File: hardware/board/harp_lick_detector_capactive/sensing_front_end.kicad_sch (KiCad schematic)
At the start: 23 parts

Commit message: loosely place components
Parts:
- C32, C33, C34, C35: Link https://www.digikey.com/en/products/detail/samsung-electro-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 -> https://www.digikey.com/en/products/detail/walsin-technolog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; Manufacturer Samsung Electro-Mechanics -> Walson Technology Corporation; Manufacturer Number CL10B104KB8NNWC -> 0402B104K160CT; Rated Voltage 50V -> 16V
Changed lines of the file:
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@@
       (effects (font (size 1.27 1.27)) hide)
     )
-    (property "Datasheet" "https://media.digikey.com/pdf/Data%20Sheets/Samsung%20PDFs/CL10B104KB8NNWC_Spec.pdf" (id 3) (at 24.13 172.72 0)
-      (effects (font (size 1.27 1.27)) hide)
-    )
-    (property "Link" "https://www.digikey.com/en/products/detail/samsung-electro-mechanics/CL10B104KB8NNWC/3887593" (id 4) (at 24.13 172.72 0)
-      (effects (font (size 1.27 1.27)) hide)
-    )
-    (property "Manufacturer" "Samsung Electro-Mechanics" (id 5) (at 24.13 172.72 0)
-      (effects (font (size 1.27 1.27)) hide)
-    )
-    (property "Manufacturer Number" "CL10B104KB8NNWC" (id 6) (at 24.13 172.72 0)
-      (effects (font (size 1.27 1.27)) hide)
-    )
-    (property "Rated Voltage" "50V" (id 7) (at 24.13 172.72 0)
+    (property "Datasheet" "http://www.passivecomponent.com/wp-content/uploads/datasheet/WTC_MLCC_General_Purpose.pdf" (id 3) (at 24.13 172.72 0)
+      (effects (font (size 1.27 1.27)) hide)
+    )
+    (property "Link" "https://www.digikey.com/en/products/detail/walsin-technology-corporation/0402B104K160CT/6707534" (id 4) (at 24.13 172.72 0)
+      (effects (font (size 1.27 1.27)) hide)
+    )
+    (property "Manufacturer" "Walson Technology Corporation" (id 5) (at 24.13 172.72 0)
+      (effects (font (size 1.27 1.27)) hide)
+    )
+    (property "Manufacturer Number" "0402B104K160CT" (id 6) (at 24.13 172.72 0)
+      (effects (font (size 1.27 1.27)) hide)
+    )
+    (property "Rated Voltage" "16V" (id 7) (at 24.13 172.72 0)
       (effects (font (size 1.27 1.27)) hide)
     )
@@
       (effects (font (size 1.27 1.27)) hide)
     )
-    (property "Datasheet" "https://media.digikey.com/pdf/Data%20Sheets/Samsung%20PDFs/CL10B104KB8NNWC_Spec.pdf" (id 3) (at 53.34 172.72 0)
-      (effects (font (size 1.27 1.27)) hide)
-    )
-    (property "Link" "https://www.digikey.com/en/products/detail/samsung-electro-mechanics/CL10B104KB8NNWC/3887593" (id 4) (at 53.34 172.72 0)
-      (effects (font (size 1.27 1.27)) hide)
-    )
-    (property "Manufacturer" "Samsung Electro-Mechanics" (id 5) (at 53.34 172.72 0)
-      (effects (font (size 1.27 1.27)) hide)
-    )
-    (property "Manufacturer Number" "CL10B104KB8NNWC" (id 6) (at 53.34 172.72 0)
-      (effects (font (size 1.27 1.27)) hide)
-    )
-    (property "Rated Voltage" "50V" (id 7) (at 53.34 172.72 0)
+    (property "Datasheet" "http://www.passivecomponent.com/wp-content/uploads/datasheet/WTC_MLCC_General_Purpose.pdf" (id 3) (at 53.34 172.72 0)
+      (effects (font (size 1.27 1.27)) hide)
+    )
+    (property "Link" "https://www.digikey.com/en/products/detail/walsin-technology-corporation/0402B104K160CT/6707534" (id 4) (at 53.34 172.72 0)
+      (effects (font (size 1.27 1.27)) hide)
+    )
+    (property "Manufacturer" "Walson Technology Corporation" (id 5) (at 53.34 172.72 0)
+      (effects (font (size 1.27 1.27)) hide)
+    )
+    (property "Manufacturer Number" "0402B104K160CT" (id 6) (at 53.34 172.72 0)
+      (effects (font (size 1.27 1.27)) hide)
+    )
+    (property "Rated Voltage" "16V" (id 7) (at 53.34 172.72 0)
       (effects (font (size 1.27 1.27)) hide)
     )
@@
       (effects (font (size 1.27 1.27)) hide)
     )
-    (property "Datasheet" "https://media.digikey.com/pdf/Data%20Sheets/Samsung%20PDFs/CL10B104KB8NNWC_Spec.pdf" (id 3) (at 53.34 182.88 0)
-      (effects (font (size 1.27 1.27)) hide)
-    )
-    (property "Link" "https://www.digikey.com/en/products/detail/samsung-electro-mechanics/CL10B104KB8NNWC/3887593" (id 4) (at 53.34 182.88 0)
-      (effects (font (size 1.27 1.27)) hide)
-    )
-    (property "Manufacturer" "Samsung Electro-Mechanics" (id 5) (at 53.34 182.88 0)
-      (effects (font (size 1.27 1.27)) hide)
-    )
-    (property "Manufacturer Number" "CL10B104KB8NNWC" (id 6) (at 53.34 182.88 0)
-      (effects (font (size 1.27 1.27)) hide)
-    )
-    (property "Rated Voltage" "50V" (id 7) (at 53.34 182.88 0)
+    (property "Datasheet" "http://www.passivecomponent.com/wp-content/uploads/datasheet/WTC_MLCC_General_Purpose.pdf" (id 3) (at 53.34 182.88 0)
+      (effects (font (size 1.27 1.27)) hide)
+    )
+    (property "Link" "https://www.digikey.com/en/products/detail/walsin-technology-corporation/0402B104K160CT/6707534" (id 4) (at 53.34 182.88 0)
+      (effects (font (size 1.27 1.27)) hide)
+    )
+    (property "Manufacturer" "Walson Technology Corporation" (id 5) (at 53.34 182.88 0)
+      (effects (font (size 1.27 1.27)) hide)
+    )
+    (property "Manufacturer Number" "0402B104K160CT" (id 6) (at 53.34 182.88 0)
+      (effects (font (size 1.27 1.27)) hide)
+    )
+    (property "Rated Voltage" "16V" (id 7) (at 53.34 182.88 0)
       (effects (font (size 1.27 1.27)) hide)
     )
@@
       (effects (font (size 1.27 1.27)) hide)
     )
-    (property "Datasheet" "https://media.digikey.com/pdf/Data%20Sheets/Samsung%20PDFs/CL10B104KB8NNWC_Spec.pdf" (id 3) (at 24.13 182.88 0)
-      (effects (font (size 1.27 1.27)) hide)
-    )
-    (property "Link" "https://www.digikey.com/en/products/detail/samsung-electro-mechanics/CL10B104KB8NNWC/3887593" (id 4) (at 24.13 182.88 0)
-      (effects (font (size 1.27 1.27)) hide)
-    )
-    (property "Manufacturer" "Samsung Electro-Mechanics" (id 5) (at 24.13 182.88 0)
-      (effects (font (size 1.27 1.27)) hide)
-    )
-    (property "Manufacturer Number" "CL10B104KB8NNWC" (id 6) (at 24.13 182.88 0)
-      (effects (font (size 1.27 1.27)) hide)
-    )
-    (property "Rated Voltage" "50V" (id 7) (at 24.13 182.88 0)
-      (effects (font (size 1.27 1.27)) hide)
-    )
+    (property "Datasheet" "http://www.passivecomponent.com/wp-content/uploads/datasheet/WTC_MLCC_General_Purpose.pdf" (id 3) (at 24.13 182.88 0)
+      (effects (font (size 1.27 1.27)) hide)
+    )
+    (property "Link" "https://www.digikey.com/en/products/detail/walsin-technology-corporation/0402B104K160CT/6707534" (id 4) (at 24.13 182.88 0)
+      (effects (font (size 1.27 1.27)) hide)
+    )
+    (property "Manufacturer" "Walson Technology Corporation" (id 5) (at 24.13 182.88 0)
+      (effects (font (size 1.27 1.27)) hide)
+    )
+    (property "Manufacturer Number" "0402B104K160CT" (id 6) (at 24.13 182.88 0)
+      (effects (font (size 1.27 1.27)) hide)
+    )
+    (property "Rated Voltage" "16V" (id 7) (at 24.13 182.88 0)
+      (effects (font (size 1.27 1.27)) hide)
+    )

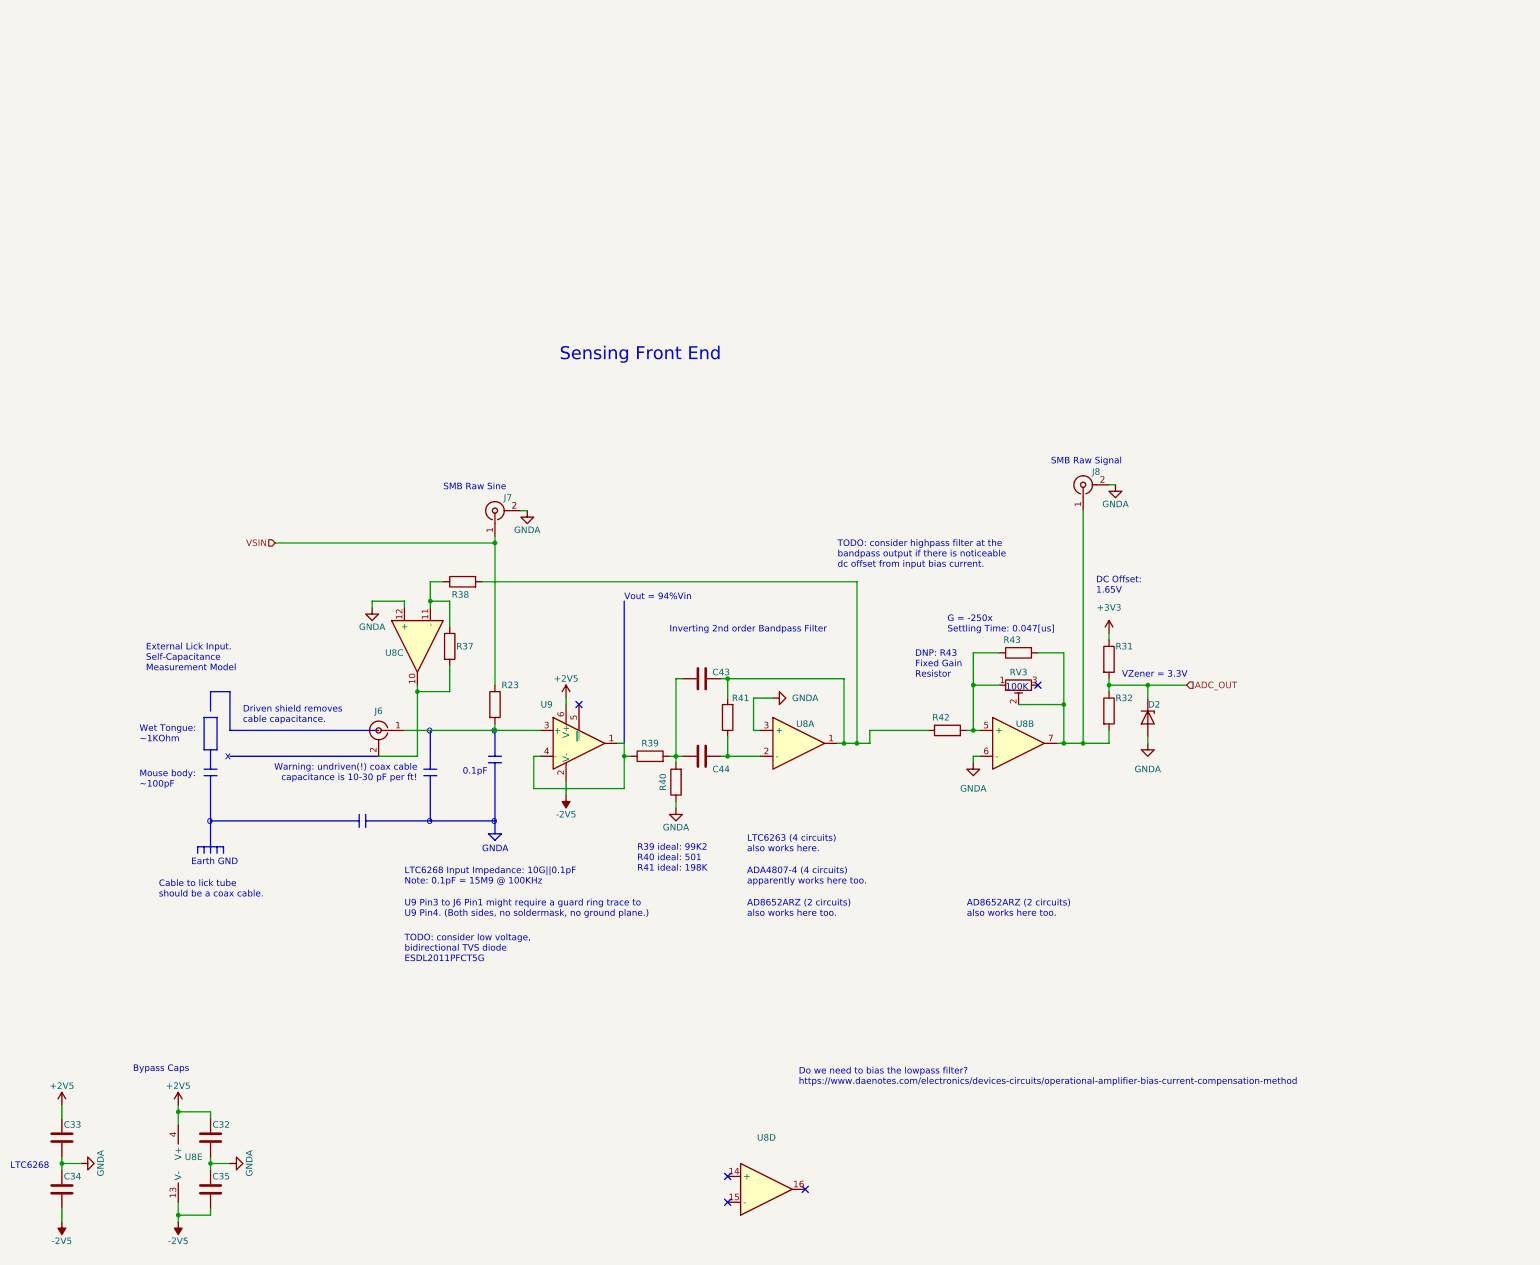
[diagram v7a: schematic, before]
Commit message: change usb connector; more layout
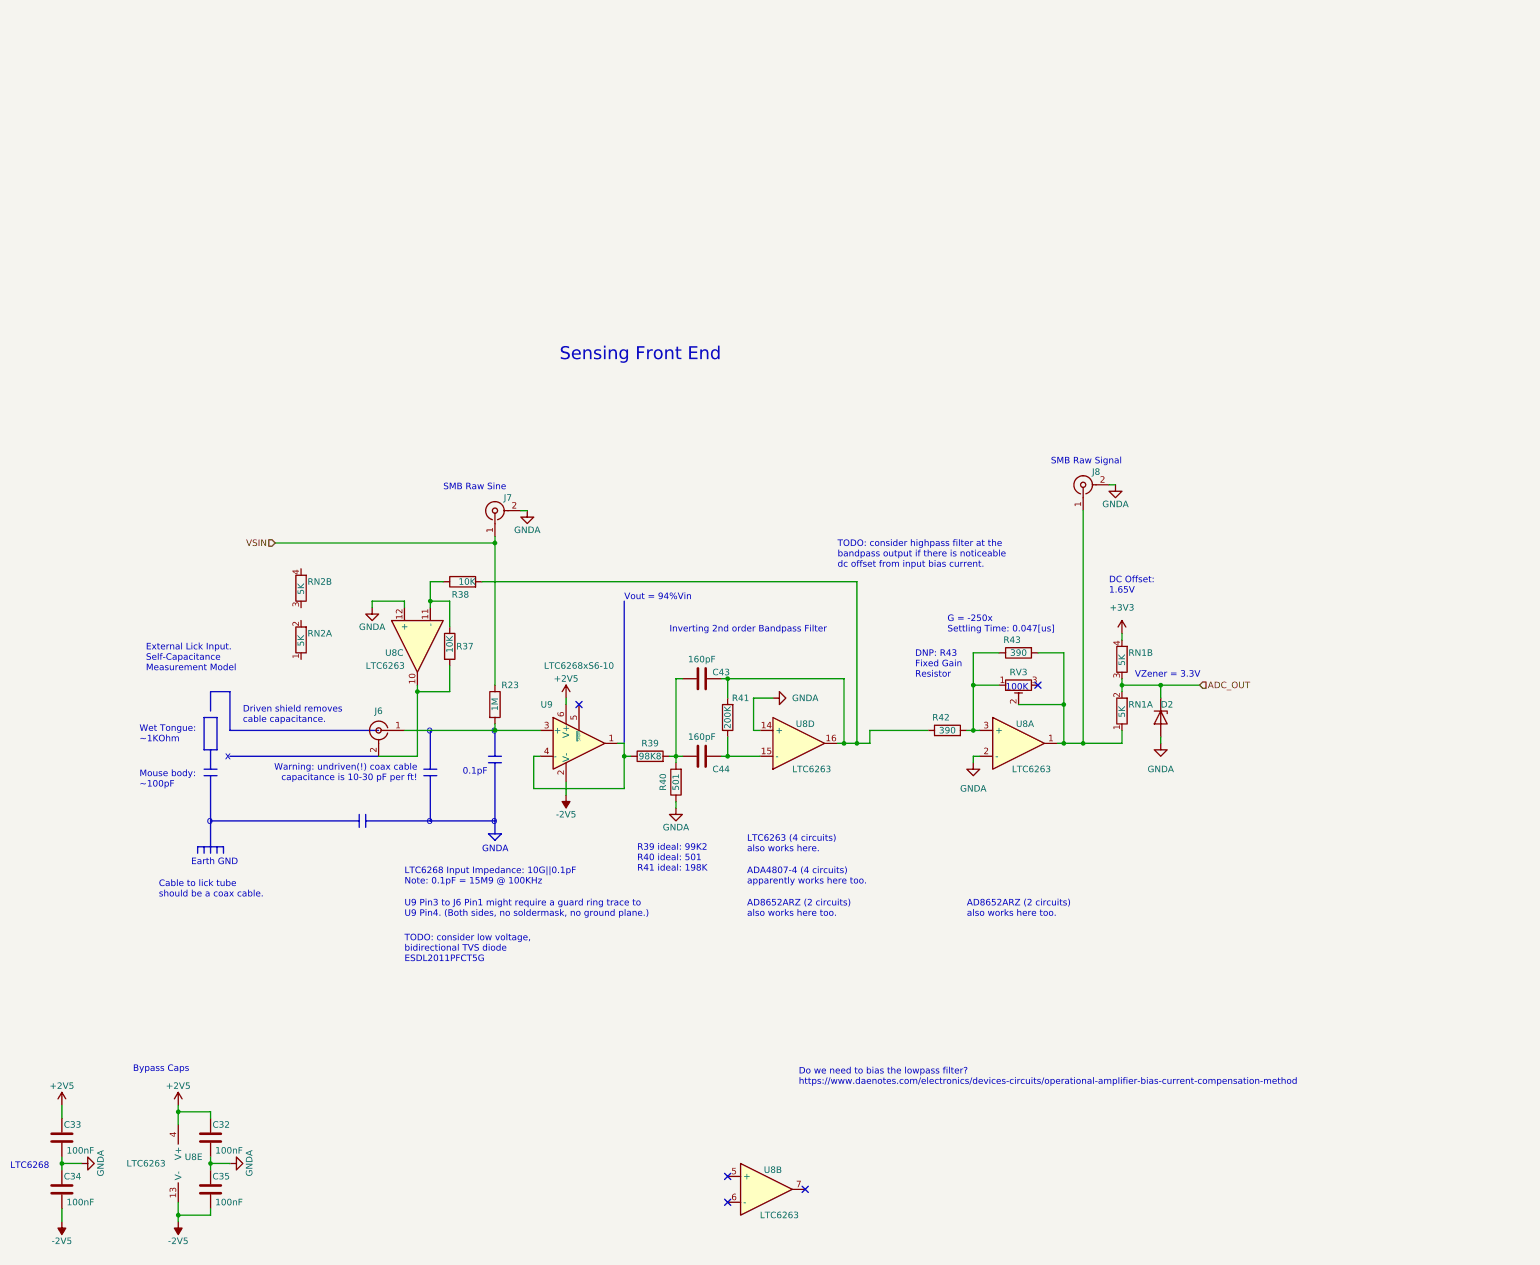
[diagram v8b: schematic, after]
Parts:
- removed R31, R32: (no value), symbol Device:R
- added RN1, RN2: 5K, Resistor_SMD:R_Array_Convex_2x0606, symbol Device:R_Pack02_SIP_Split
- C32, C33, C34, C35: value (none) -> 100nF; footprint (none) -> Capacitor_SMD:C_0402_1005Metric_Pad0.74x0.62mm_HandSolder
- C43, C44: value (none) -> 160pF; footprint (none) -> Capacitor_SMD:C_0402_1005Metric_Pad0.74x0.62mm_HandSolder
- D2: value (none) -> BZX384-A3V3-QX; footprint (none) -> Diode_SMD:D_SOD-323_HandSoldering
- J6: value (none) -> Conn_Coaxial; footprint (none) -> machine_agency_components:conn_bnc_receptacle_50ohm
- J7, J8: value (none) -> Conn_Coaxial; footprint (none) -> Connector_Coaxial:SMA_Amphenol_901-143_Horizontal
- R23: value (none) -> 1M; footprint (none) -> Resistor_SMD:R_0603_1608Metric_Pad0.98x0.95mm_HandSolder
- R37, R38: value (none) -> 10K; footprint (none) -> Resistor_SMD:R_0402_1005Metric_Pad0.72x0.64mm_HandSolder
- R39: value (none) -> 98K8; footprint (none) -> Resistor_SMD:R_0603_1608Metric_Pad0.98x0.95mm_HandSolder
- R40: value (none) -> 501; footprint (none) -> Resistor_SMD:R_0603_1608Metric_Pad0.98x0.95mm_HandSolder
- R41: value (none) -> 200K; footprint (none) -> Resistor_SMD:R_0603_1608Metric_Pad0.98x0.95mm_HandSolder
- R42, R43: value (none) -> 390; footprint (none) -> Resistor_SMD:R_0603_1608Metric_Pad0.98x0.95mm_HandSolder
- RV3: value (none) -> R_Potentiometer_Trim; footprint (none) -> Potentiometer_SMD:Potentiometer_Bourns_3314G_Vertical
- U8: value (none) -> LTC6263; footprint (none) -> Package_SO:MSOP-16_3x4mm_P0.5mm
- U9: value (none) -> LTC6268xS6-10; footprint (none) -> Package_TO_SOT_SMD:SOT-23-6_Handsoldering
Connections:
- net +3V3: now also RN1.4 (R2.2)
- net ADC_OUT: now also RN1.2 (R1.2), RN1.3 (R2.1)
- net GNDA: now also U8.14 (+), U8.2 (-); no longer U8.3 (+), U8.6 (-)
- net at R42.2, R43.1, RV3.1: now also U8.3 (+); no longer U8.5 (+)
- net at J8.1 (In), R43.2, RV3.2: now also U8.1, RN1.1 (R1.1); no longer U8.7
- net at C44.2, R41.1: now also U8.15 (-); no longer U8.2 (-)
- net at C43.2, R38.2, R41.2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: now also U8.16; no longer U8.1
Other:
- moved on the sheet: D2, U8A, U8B, U8D
